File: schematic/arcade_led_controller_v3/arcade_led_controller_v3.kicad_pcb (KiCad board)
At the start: 2 copper layers, 104.1 x 70 mm, 62 parts, among them J1 GND_BUS_1, J2 GND_BUS_2, J3 PSU_GND_BUS, P1_BALLTOP_LED_1 WS2812B, P1_BUTTONS_LED1 WS2812B, P1_DP_JOY_MODE_LED1 LED, P1_JOYSTICK_LED1 WS2812B, P1_LS_JOY_MODE_LED1 LED, P1_RS_JOY_MODE_LED1 LED, P2_BALLTOP_LED_1 WS2812B, P2_BUTTONS_LED1 WS2812B, P2_DP_JOY_MODE_LED1 LED, P2_JOYSTICK_LED1 WS2812B, P2_LS_JOY_MODE_LED1 LED, P2_RS_JOY_MODE_LED1 LED, Q1 Q_NMOS_GDS, Q2 Q_NMOS_GDS, Q3 Q_NMOS_GDS, Q4(PN2222)1 PN2222A, Q5(PN222)1 PN2222A, Q6(PN2222)1 PN2222A, Q7(PN2222)1 PN2222A, U1 74AHCT125, U2 74AHCT125, U3 EA_DOGL128X-6

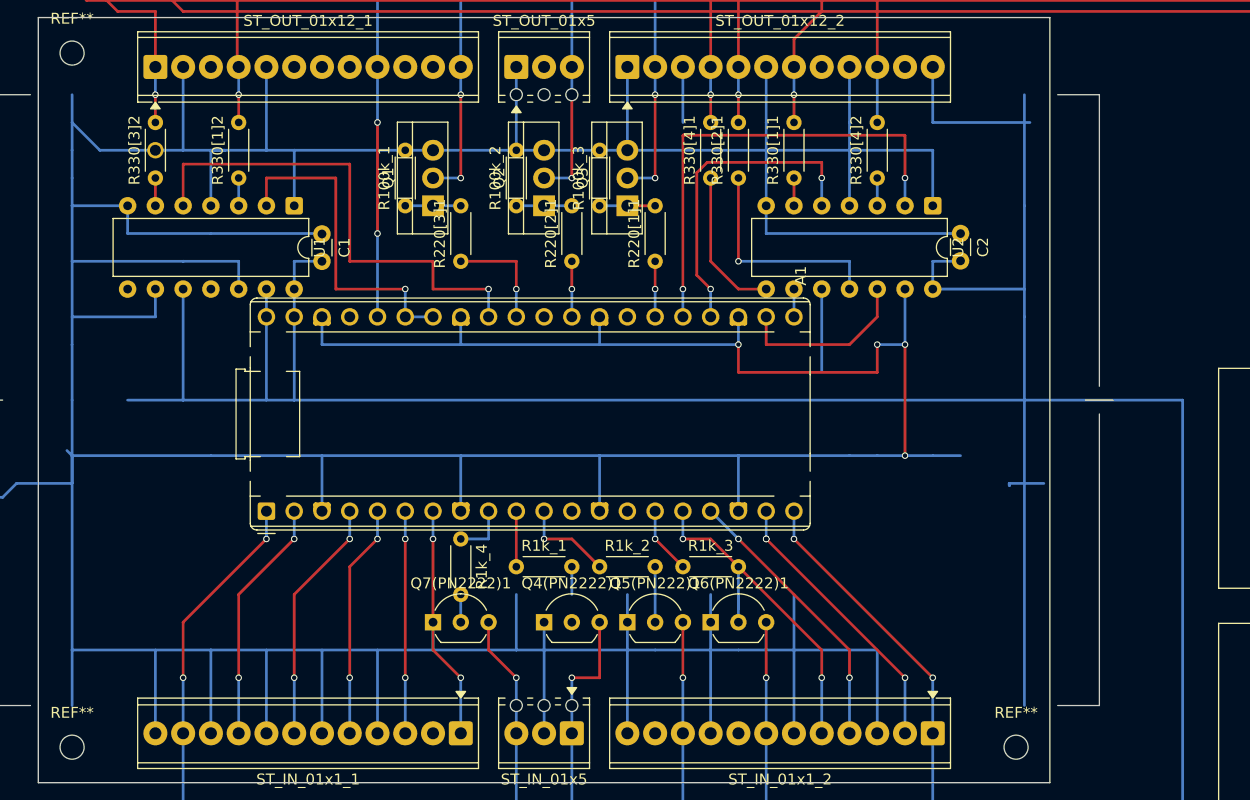
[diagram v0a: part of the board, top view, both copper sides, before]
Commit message: replace pico footprint with 1x20 pin header sockets
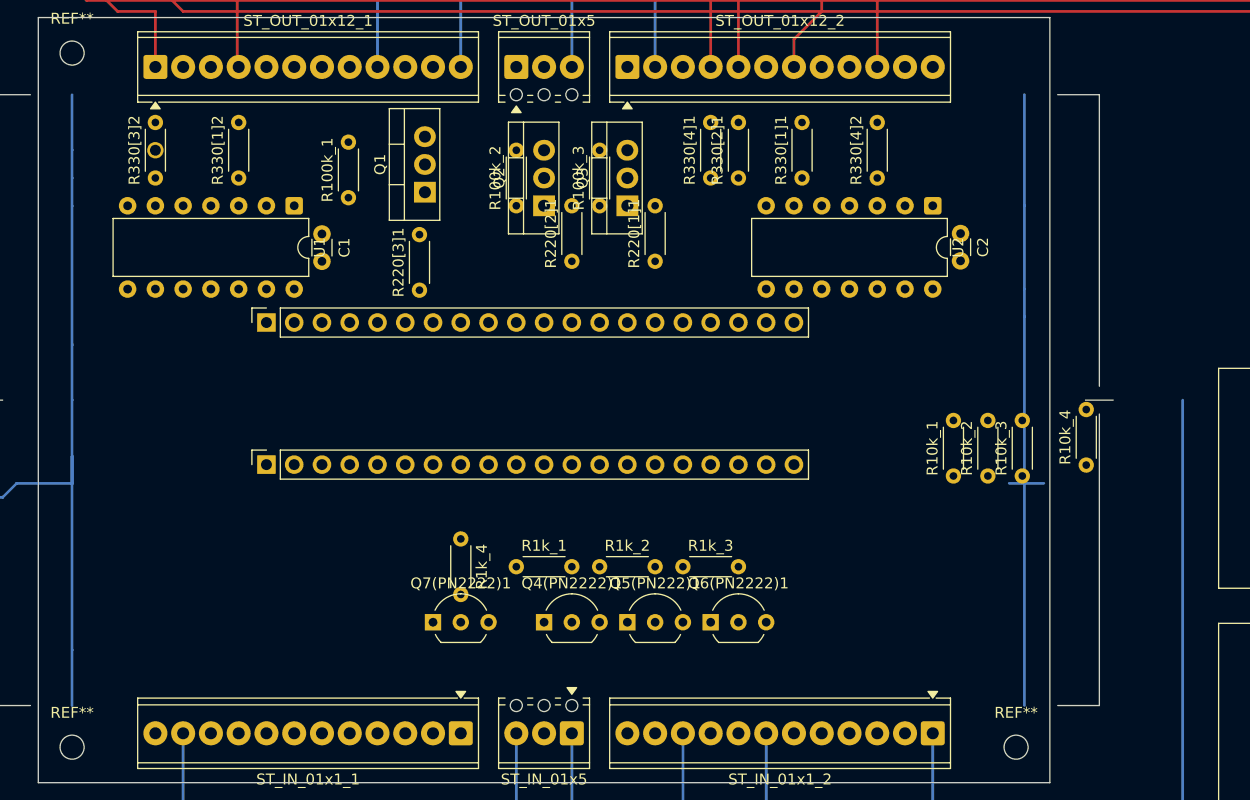
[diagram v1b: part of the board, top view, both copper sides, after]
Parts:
- removed A1: RaspberryPi_Pico, Module:RaspberryPi_Pico_Common_THT
- added J4: Pico_Socket_Row_2, Connector_PinSocket_2.54mm:PinSocket_1x20_P2.54mm_Vertical, F.Cu at (127.0, 94.5)
- added J5: Pico_Socket_Row_1, Connector_PinSocket_2.54mm:PinSocket_1x20_P2.54mm_Vertical, F.Cu at (127.0, 107.5)
- added R10k_1: 10kΩ, Resistor_THT:R_Axial_DIN0204_L3.6mm_D1.6mm_P5.08mm_Horizontal, F.Cu at (189.8, 108.5)
- added R10k_2: 10kΩ, Resistor_THT:R_Axial_DIN0204_L3.6mm_D1.6mm_P5.08mm_Horizontal, F.Cu at (193.0, 108.5)
- added R10k_3: 10kΩ, Resistor_THT:R_Axial_DIN0204_L3.6mm_D1.6mm_P5.08mm_Horizontal, F.Cu at (196.2, 108.5)
- added R10k_4: 10kΩ, Resistor_THT:R_Axial_DIN0204_L3.6mm_D1.6mm_P5.08mm_Horizontal, F.Cu at (202.0, 107.5)
- moved R100k_1 5.25 mm to (134.5, 83.1)
- moved R220[3]1 4.61 mm to (141.0, 91.5)
- moved Q1 1.44 mm to (141.5, 82.6)
- moved R330[1]1 0.74 mm to (176.0, 81.3)
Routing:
- net GND: track 1795.4 -> 1202.3 mm, vias 4 -> 0
- net +5V: track 1226.2 -> 1024.7 mm
- net /2A(2): track 45.7 -> 0.00 mm, vias 1 -> 0
- net /1A: track 43.4 -> 0.00 mm, vias 2 -> 0
- net /DISPLAY_DC: track 20.3 -> 59.1 mm, vias 2 -> 0
- net /1A(2): track 30.5 -> 0.00 mm, vias 1 -> 0
- net /2A: track 29.5 -> 0.00 mm, vias 2 -> 0
- net /ROTARY_SW: track 27.1 -> 0.00 mm, vias 2 -> 0
- net /ROTARY_DT: track 25.6 -> 0.00 mm, vias 2 -> 0
- net /DISPLAY_RST: track 176.2 -> 150.6 mm, vias 2 -> 0
- net /ROTARY_CLK: track 25.6 -> 0.00 mm, vias 3 -> 0
- net /DISPLAY_CS: track 83.5 -> 60.0 mm, vias 2 -> 0
- net /DISPLAY_VSS: track 222.2 -> 199.4 mm, vias 2 -> 0
- net /DISPLAY_SCK: track 22.4 -> 0.00 mm, vias 2 -> 0
- net /P1_SIG: track 22.4 -> 0.00 mm, vias 2 -> 0
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
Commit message: Update tracks
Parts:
- removed the REF** at (116.8, 78.7)
- added REF**: MountingHole_2.2mm_M2, MountingHole:MountingHole_2.2mm_M2, F.Cu at (195.6, 69.8)
- moved R220[3]1 87.6 mm to (55.6, 72.4)
- moved J4 48.3 mm to (175.3, 96.5), turned to -90 degrees
- moved R330[1]2 35.6 mm to (160.0, 81.3)
- moved R330[3]2 35.6 mm to (152.4, 81.3)
- moved U1 35.6 mm to (165.1, 83.8)
- moved C1 35.6 mm to (167.6, 86.4)
- moved R100k_2 26.0 mm to (124.1, 87.6)
- moved R100k_3 24.1 mm to (133.7, 87.6)
- moved Q1 23.5 mm to (118.3, 86.4)
- moved Q2 23.5 mm to (129.2, 87.6)
- moved Q3 23.5 mm to (136.8, 87.6)
- moved R220[1]1 23.5 mm to (139.4, 92.7)
- moved R220[2]1 23.5 mm to (131.8, 92.7)
- moved R100k_1 22.0 mm to (112.7, 86.4)
- moved R330[4]1 19.1 mm to (186.7, 81.3)
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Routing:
- net GND: track 1202.3 -> 1474.7 mm
- net /DISPLAY_DC: track 59.1 -> 0.00 mm
- net /4A: track 0.00 -> 56.7 mm
- net +5V: track 1024.7 -> 1075.8 mm
- net /3A: track 0.00 -> 37.4 mm
- net /1A: track 0.00 -> 24.1 mm
- net /2Y: track 0.00 -> 24.0 mm
- net /3Y: track 0.00 -> 23.9 mm
- net /P1_DP_CATHODE: track 20.8 -> 0.00 mm
- net /P1_RS_CATHODE: track 20.3 -> 0.00 mm
- net /2A: track 0.00 -> 20.1 mm
- net /1Y: track 0.00 -> 18.7 mm
- net ROTARY_+5V: track 0.00 -> 17.4 mm
- net /P2_BUTTON_DATA: track 24.0 -> 8.26 mm
- net /ACCENT_DATA: track 50.8 -> 35.5 mm
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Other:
- board size 104.1 x 70 mm -> 102.9 x 70 mm

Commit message: More routing updates
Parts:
- moved R220[3]1 90.0 mm to (143.5, 91.6)
- moved U1 53.2 mm to (111.9, 85.0), turned to 0 degrees
- moved C1 48.3 mm to (119.5, 82.0), turned to 0 degrees
- moved R330[3]2 35.4 mm to (117.0, 82.0)
- moved R330[1]2 34.0 mm to (126.0, 81.0)
- moved R220[1]1 30.2 mm to (169.5, 90.0)
- moved Q3 29.2 mm to (165.9, 85.0)
- moved R1k_1 29.1 mm to (120.8, 116.3)
- moved Q4(PN2222)1 29.1 mm to (123.3, 121.4)
- moved Q5(PN222)1 29.1 mm to (131.0, 121.4)
- moved Q7(PN2222)1 29.1 mm to (113.2, 121.4)
- moved R10k_1 29.1 mm to (150.6, 119.8)
- moved R10k_2 29.1 mm to (153.7, 119.8)
- moved R1k_2 29.1 mm to (128.4, 116.3)
- moved R1k_3 29.1 mm to (136.0, 116.3)
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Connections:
- ACCENT_LED1 pad 4: /ACCENT_DATA -> unconnected-(ACCENT_LED1-DIN-Pad4)
- OPTIONS_BUTTONS_LED1 pad 3: /OPTIONS_LED_DATA -> unconnected-(OPTIONS_BUTTONS_LED1-DIN-Pad3)
- P1_BUTTONS_LED1 pad 3: /P1_BUTTON_DATA -> unconnected-(P1_BUTTONS_LED1-DIN-Pad3)
- P1_JOYSTICK_LED1 pad 3: /P1_JOYSTICK_DATA -> unconnected-(P1_JOYSTICK_LED1-DIN-Pad3)
- ST_OUT_01x12_1 pad 7: unconnected-(ST_OUT_01x12_1-Pin_7-Pad7) -> /DISPLAY_VSS
- ST_OUT_01x12_1 pad 9: /DISPLAY_VSS -> GND
- ST_OUT_01x12_2 pad 10: /OPTIONS_LED_DATA -> /P1_BUTTON_DATA
- ST_OUT_01x12_2 pad 11: unconnected-(ST_OUT_01x12_2-Pin_11-Pad11) -> /P1_JOYSTICK_DATA
- ST_OUT_01x12_2 pad 3: GND -> unconnected-(ST_OUT_01x12_2-Pin_3-Pad3)
- ST_OUT_01x12_2 pad 4: /P1_BUTTON_DATA -> unconnected-(ST_OUT_01x12_2-Pin_4-Pad4)
- ST_OUT_01x12_2 pad 5: /P1_JOYSTICK_DATA -> GND
- ST_OUT_01x12_2 pad 6: GND -> /OPTIONS_LED_DATA
- ST_OUT_01x12_2 pad 7: /ACCENT_DATA -> GND
- ST_OUT_01x12_2 pad 8: unconnected-(ST_OUT_01x12_2-Pin_8-Pad8) -> /ACCENT_DATA
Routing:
- net GND: track 1474.7 -> 1792.1 mm
- net +5V: track 1075.8 -> 1174.4 mm
- net /2A(2): track 0.00 -> 75.5 mm
- net /1A(2): track 0.00 -> 67.9 mm
- net /DISPLAY_RST: track 150.6 -> 180.5 mm
- net /ROTARY_SW: track 0.00 -> 29.8 mm
- net /ROTARY_DT: track 0.00 -> 29.8 mm
- net /ROTARY_CLK: track 0.00 -> 29.8 mm
- net /ACCENT_DATA: track 35.5 -> 5.75 mm
- net /DISPLAY_VSS: track 190.5 -> 218.0 mm
- net /1Y(2): track 0.00 -> 24.8 mm
- net /2Y(2): track 0.00 -> 18.4 mm
- net ROTARY_+5V: track 17.4 -> 0.00 mm
- net /P1_LS_CATHODE: track 14.0 -> 29.5 mm
- net /P1_DP_CATHODE: track 0.00 -> 15.3 mm
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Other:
- outline, holes or cut-outs redrawn

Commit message: Add power LED connections, and replace pn2222 transistors with MOSFETs
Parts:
- removed +12V_BUS_1, +12V_BUS_2: Conn_01x05_Pin, TerminalBlock_WAGO:TerminalBlock_WAGO_233-505_2x05_P2.54mm
- removed +5V_BUS_1, +5V_BUS_2: Conn_01x05_Pin, Connector_Wago:Wago_734-165_1x05_P3.50mm_Horizontal
- removed ACCENT_LED1: WS2811, LED_SMD:LED_WS2812B_PLCC4_5.0x5.0mm_P3.2mm
- removed ATX_PSU_1: ATX-24, Connector_Molex:Molex_Mini-Fit_Jr_5566-24A_2x12_P4.20mm_Vertical
- removed J1: GND_BUS_1, TerminalBlock_WAGO:TerminalBlock_WAGO_233-506_2x06_P2.54mm
- removed J2: GND_BUS_2, TerminalBlock_WAGO:TerminalBlock_WAGO_233-504_2x04_P2.54mm
- removed J3: PSU_GND_BUS, Connector_Wago:Wago_734-163_1x03_P3.50mm_Horizontal
- removed OPTIONS_BUTTONS_LED1, P1_BALLTOP_LED_1, P1_BUTTONS_LED1, P1_JOYSTICK_LED1, P2_BALLTOP_LED_1, P2_BUTTONS_LED1, P2_JOYSTICK_LED1: WS2812B, LED_SMD:LED_WS2812B-2020_PLCC4_2.0x2.0mm
- removed P1_DP_JOY_MODE_LED1, P1_LS_JOY_MODE_LED1, P1_RS_JOY_MODE_LED1, P2_DP_JOY_MODE_LED1, P2_LS_JOY_MODE_LED1, P2_RS_JOY_MODE_LED1, REC_LED1: LED, LED_THT:LED_D1.8mm_W1.8mm_H2.4mm_Horizontal_O3.81mm_Z1.6mm
- removed Q4(PN2222)1, Q5(PN222)1, Q6(PN2222)1, Q7(PN2222)1: PN2222A, Package_TO_SOT_THT:TO-92_Inline_Wide
- removed R10k_1, R10k_2, R10k_3, R10k_4: 10kΩ, Resistor_THT:R_Axial_DIN0204_L3.6mm_D1.6mm_P5.08mm_Horizontal
- removed R1k_1, R1k_2, R1k_3, R1k_4: 1kΩ, Resistor_THT:R_Axial_DIN0204_L3.6mm_D1.6mm_P5.08mm_Horizontal
- removed U3: EA_DOGL128X-6, Display:EA_DOGL128-6
- added J_PWR_IN1: Conn_01x02, Connector_Molex:Molex_SL_171971-0002_1x02_P2.54mm_Vertical, F.Cu at (195.9, 121.4)
- added Q4: Q_NMOS_GDS, Package_TO_SOT_THT:TO-220-3_Vertical, F.Cu at (138.0, 120.0)
- added Q5: Q_NMOS_GDS, Package_TO_SOT_THT:TO-220-3_Vertical, F.Cu at (146.0, 120.0)
- added Q6: Q_NMOS_GDS, Package_TO_SOT_THT:TO-220-3_Vertical, F.Cu at (154.5, 120.0)
- added Q7: Q_NMOS_GDS, Package_TO_SOT_THT:TO-220-3_Vertical, F.Cu at (163.5, 120.5)
- added Q8: Q_NMOS_GDS, Package_TO_SOT_THT:TO-220-3_Vertical, F.Cu at (171.5, 120.5)
- added R100k_4: 100kΩ, Resistor_THT:R_Axial_DIN0204_L3.6mm_D1.6mm_P5.08mm_Horizontal, F.Cu at (135.0, 125.1)
- added R100k_5: 100kΩ, Resistor_THT:R_Axial_DIN0204_L3.6mm_D1.6mm_P5.08mm_Horizontal, F.Cu at (143.0, 125.0)
- added R100k_6: 100kΩ, Resistor_THT:R_Axial_DIN0204_L3.6mm_D1.6mm_P5.08mm_Horizontal, F.Cu at (151.5, 125.1)
- added R100k_7: 100kΩ, Resistor_THT:R_Axial_DIN0204_L3.6mm_D1.6mm_P5.08mm_Horizontal, F.Cu at (160.5, 125.6)
- added R100k_8: 100kΩ, Resistor_THT:R_Axial_DIN0204_L3.6mm_D1.6mm_P5.08mm_Horizontal, F.Cu at (168.5, 126.6)
- added R220_4: 220Ω, Resistor_THT:R_Axial_DIN0204_L3.6mm_D1.6mm_P5.08mm_Horizontal, F.Cu at (148.0, 116.1)
- added R220_5: 220Ω, Resistor_THT:R_Axial_DIN0204_L3.6mm_D1.6mm_P5.08mm_Horizontal, F.Cu at (151.5, 116.1)
- added R220_6: 220Ω, Resistor_THT:R_Axial_DIN0204_L3.6mm_D1.6mm_P5.08mm_Horizontal, F.Cu at (154.5, 116.0)
- added R220_7: 220Ω, Resistor_THT:R_Axial_DIN0204_L3.6mm_D1.6mm_P5.08mm_Horizontal, F.Cu at (160.0, 116.1)
- added R220_8: 220Ω, Resistor_THT:R_Axial_DIN0204_L3.6mm_D1.6mm_P5.08mm_Horizontal, F.Cu at (165.0, 115.8)
- added R330[3]3: 330Ω, Resistor_THT:R_Axial_DIN0204_L3.6mm_D1.6mm_P5.08mm_Horizontal, F.Cu at (126.5, 81.1)
- moved R330[4]1 18.0 mm to (178.5, 97.6)
- moved R330[1]1 16.6 mm to (181.0, 97.6)
- moved R330[1]2 11.0 mm to (115.0, 81.1)
- moved R330[4]2 10.1 mm to (185.5, 82.6)
- moved R330[3]2 7.06 mm to (110.0, 81.1)
- moved R100k_2 4.53 mm to (151.0, 85.6)
- moved R220_2 4.26 mm to (159.0, 91.5)
- moved Q2 4.10 mm to (155.4, 85.5)
- moved R220_1 3.16 mm to (146.5, 90.6)
- moved Q1 3.00 mm to (143.5, 85.6)
- moved R100k_1 3.00 mm to (139.0, 85.6)
- moved R330[2]1 2.31 mm to (189.0, 83.6)
- moved C1 1.50 mm to (118.0, 82.0)
- renumbered R220[3]1 to R220_1, R220[2]1 to R220_2, R220[1]1 to R220_3
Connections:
- J4 pad 27: unconnected-(J4-GP21-Pad27) -> /P1_DP_GP
- J4 pad 29: /P1_DP_GP -> /P1_RS_GP
- J4 pad 31: /PS_RS_GP -> /3A(2)
- J4 pad 36: /DISPLAY_VSS -> /PICO_3V3_OUT
- J5 pad 10: /LS_1K_TO_GP -> /REC_100K_TO_GP
- J5 pad 11: /DP_1K_TO_GP -> /LS_100K_TO_GP
- J5 pad 12: unconnected-(J5-GP9-Pad12) -> /DP_100K_TO_GP
- J5 pad 14: unconnected-(J5-GP10-Pad14) -> /RS_100K_TO_GP
- J5 pad 15: /RS_1K_TO_GP -> /PWR_100K_TO_GP
- J5 pad 9: /REC_1K_TO_GP -> unconnected-(J5-GP6-Pad9)
- R220_1 pad 1: /PS_RS_GP -> /P1_RS_GP
- R330[1]2 pad 2: /P2_BUTTON_DATA -> /ROTARY_LED_DATA
- ST_IN_01x1_1 pad 1: /P2_SIG -> /REC_LED_CATHODE
- ST_IN_01x1_1 pad 10: GND -> /P1_SIG
- ST_IN_01x1_1 pad 11: /DISPLAY_CS -> GND
- ST_IN_01x1_1 pad 12: GND -> /DISPLAY_CS
- ST_IN_01x1_1 pad 2: unconnected-(ST_IN_01x1_1-Pin_2-Pad2) -> GND
- ST_IN_01x1_1 pad 3: /DISPLAY_DC -> /P2_SIG
- ST_IN_01x1_1 pad 4: DISPLAY_GND -> /DISPLAY_DC
- ST_IN_01x1_1 pad 5: /DISPLAY_MOSI -> GND
- ST_IN_01x1_1 pad 6: GND -> /DISPLAY_MOSI
- ST_IN_01x1_1 pad 7: /DISPLAY_SCK -> GND
- ST_IN_01x1_1 pad 8: GND -> /DISPLAY_SCK
- ST_IN_01x1_1 pad 9: /P1_SIG -> GND
- ST_IN_01x1_2 pad 10: /P2_DP_CATHODE -> GND
- ST_IN_01x1_2 pad 11: unconnected-(ST_IN_01x1_2-Pin_11-Pad11) -> /P2_DP_CATHODE
- ST_IN_01x1_2 pad 5: /ROTARY_SW -> GND
- ST_IN_01x1_2 pad 6: ROTARY_GND -> /ROTARY_SW
- ST_IN_01x1_2 pad 7: /P2_RS_CATHODE -> /PWR_LED_CATHODE
- ST_IN_01x1_2 pad 8: unconnected-(ST_IN_01x1_2-Pin_8-Pad8) -> GND
- ST_IN_01x1_2 pad 9: GND -> /P2_RS_CATHODE
- ST_IN_01x5 pad 3: /REC_LED_CATHODE -> unconnected-(ST_IN_01x5-Pin_3-Pad3)
- ST_OUT_01x12_1 pad 3: unconnected-(ST_OUT_01x12_1-Pin_3-Pad3) -> /ROTARY_LED_DATA
- ST_OUT_01x12_1 pad 7: /DISPLAY_VSS -> /PICO_3V3_OUT
- ST_OUT_01x12_1 pad 8: unconnected-(ST_OUT_01x12_1-Pin_8-Pad8) -> /PICO_3V3_OUT
- ST_OUT_01x12_2 pad 10: /P1_BUTTON_DATA -> /OPTIONS_LED_DATA
- ST_OUT_01x12_2 pad 12: ROTARY_+5V -> unconnected-(ST_OUT_01x12_2-Pin_12-Pad12)
- ST_OUT_01x12_2 pad 6: /OPTIONS_LED_DATA -> /P1_BUTTON_DATA
- U1 pad 10: +5V -> GND
- U1 pad 9: GND -> /3A(2)
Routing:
- net +12V: track 1416.2 -> 0.00 mm
- net GND: track 1792.1 -> 745.3 mm
- net +5V: track 1174.4 -> 149.2 mm
- net /DISPLAY_VSS: track 218.0 -> 0.00 mm
- net /DISPLAY_RST: track 180.5 -> 29.8 mm
- net /3A(2): track 0.00 -> 41.2 mm
- net /P2_SIG: track 0.00 -> 32.5 mm
- net /DISPLAY_CS: track 60.0 -> 28.8 mm
- net /DISPLAY_DC: track 0.00 -> 30.3 mm
- net /PICO_3V3_OUT: track 0.00 -> 29.0 mm
- net /DISPLAY_MOSI: track 0.00 -> 28.0 mm
- net /DISPLAY_SCK: track 0.00 -> 27.7 mm
- net /P1_SIG: track 0.00 -> 27.7 mm
- net /3Y(2): track 0.00 -> 23.7 mm
- net /2Y: track 26.8 -> 3.76 mm
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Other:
- board size 102.9 x 70 mm -> 92.5 x 70 mm
- board text removed: "+5V"
- board text removed: "GND"
